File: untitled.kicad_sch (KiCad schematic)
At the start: 1 part, among them J1 Conn_02x20_Odd_Even

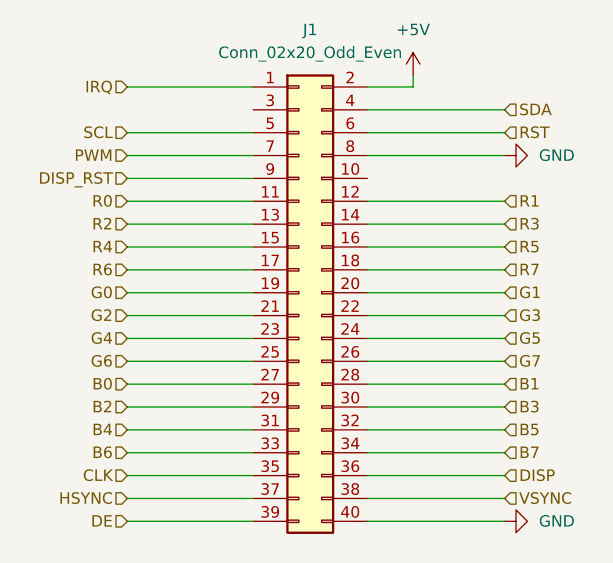
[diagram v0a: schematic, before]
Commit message: edit lcd symbol
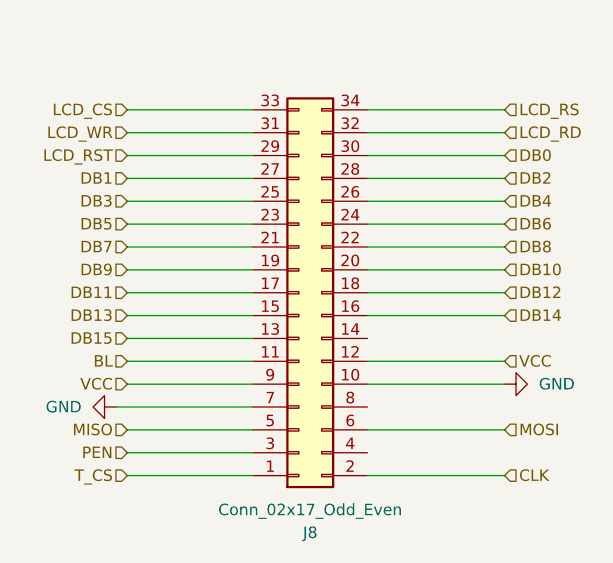
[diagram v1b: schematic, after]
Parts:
- removed J1: Conn_02x20_Odd_Even, pcbDAC:LCD, symbol Connector_Generic:Conn_02x20_Odd_Even
- added J8: Conn_02x17_Odd_Even, Connector_PinSocket_2.54mm:PinSocket_2x17_P2.54mm_Vertical, symbol Connector_Generic:Conn_02x17_Odd_Even
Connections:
- net CLK: now also J8.2 (Pin_2)
- net GND: now also J8.10 (Pin_10), J8.7 (Pin_7)
- new net BL: J8.11 (Pin_11)
- new net DB0: J8.30 (Pin_30)
- new net DB1: J8.27 (Pin_27)
- new net DB10: J8.20 (Pin_20)
- new net DB11: J8.17 (Pin_17)
- new net DB12: J8.18 (Pin_18)
- new net DB13: J8.15 (Pin_15)
- new net DB14: J8.16 (Pin_16)
- new net DB15: J8.13 (Pin_13)
- new net DB2: J8.28 (Pin_28)
- new net DB3: J8.25 (Pin_25)
- new net DB4: J8.26 (Pin_26)
- new net DB5: J8.23 (Pin_23)
- new net DB6: J8.24 (Pin_24)
- new net DB7: J8.21 (Pin_21)
- new net DB8: J8.22 (Pin_22)
- new net DB9: J8.19 (Pin_19)
- new net LCD_CS: J8.33 (Pin_33)
- new net LCD_RD: J8.32 (Pin_32)
- new net LCD_RS: J8.34 (Pin_34)
- new net LCD_RST: J8.29 (Pin_29)
- new net LCD_WR: J8.31 (Pin_31)
- new net MISO: J8.5 (Pin_5)
- new net MOSI: J8.6 (Pin_6)
- new net PEN: J8.3 (Pin_3)
- new net T_CS: J8.1 (Pin_1)
- new net VCC: J8.12 (Pin_12), J8.9 (Pin_9)

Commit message: Make 3d model for ADC and FPGA. Trying to assembly
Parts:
- J8: footprint Connector_PinSocket_2.54mm:PinSocket_2x17_P2.54mm_Vertical -> Connector_PinHeader_2.54mm:PinHeader_2x17_P2.54mm_Horizontal
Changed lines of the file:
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@@
 			)
 		)
-		(property "Footprint" "Connector_PinSocket_2.54mm:PinSocket_2x17_P2.54mm_Vertical"
+		(property "Footprint" "Connector_PinHeader_2.54mm:PinHeader_2x17_P2.54mm_Horizontal"
 			(at 118.11 78.74 0)
 			(effects
